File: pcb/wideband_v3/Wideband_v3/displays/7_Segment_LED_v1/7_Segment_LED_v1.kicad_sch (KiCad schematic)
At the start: 31 parts, among them J1 Conn_01x10, U1 4511, U10 74AUC2G04, U2 SM420561N, U3 SM420561N, U4 4511, U5 4511, U6 4511, U7 SM420561N, U8 SM420561N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

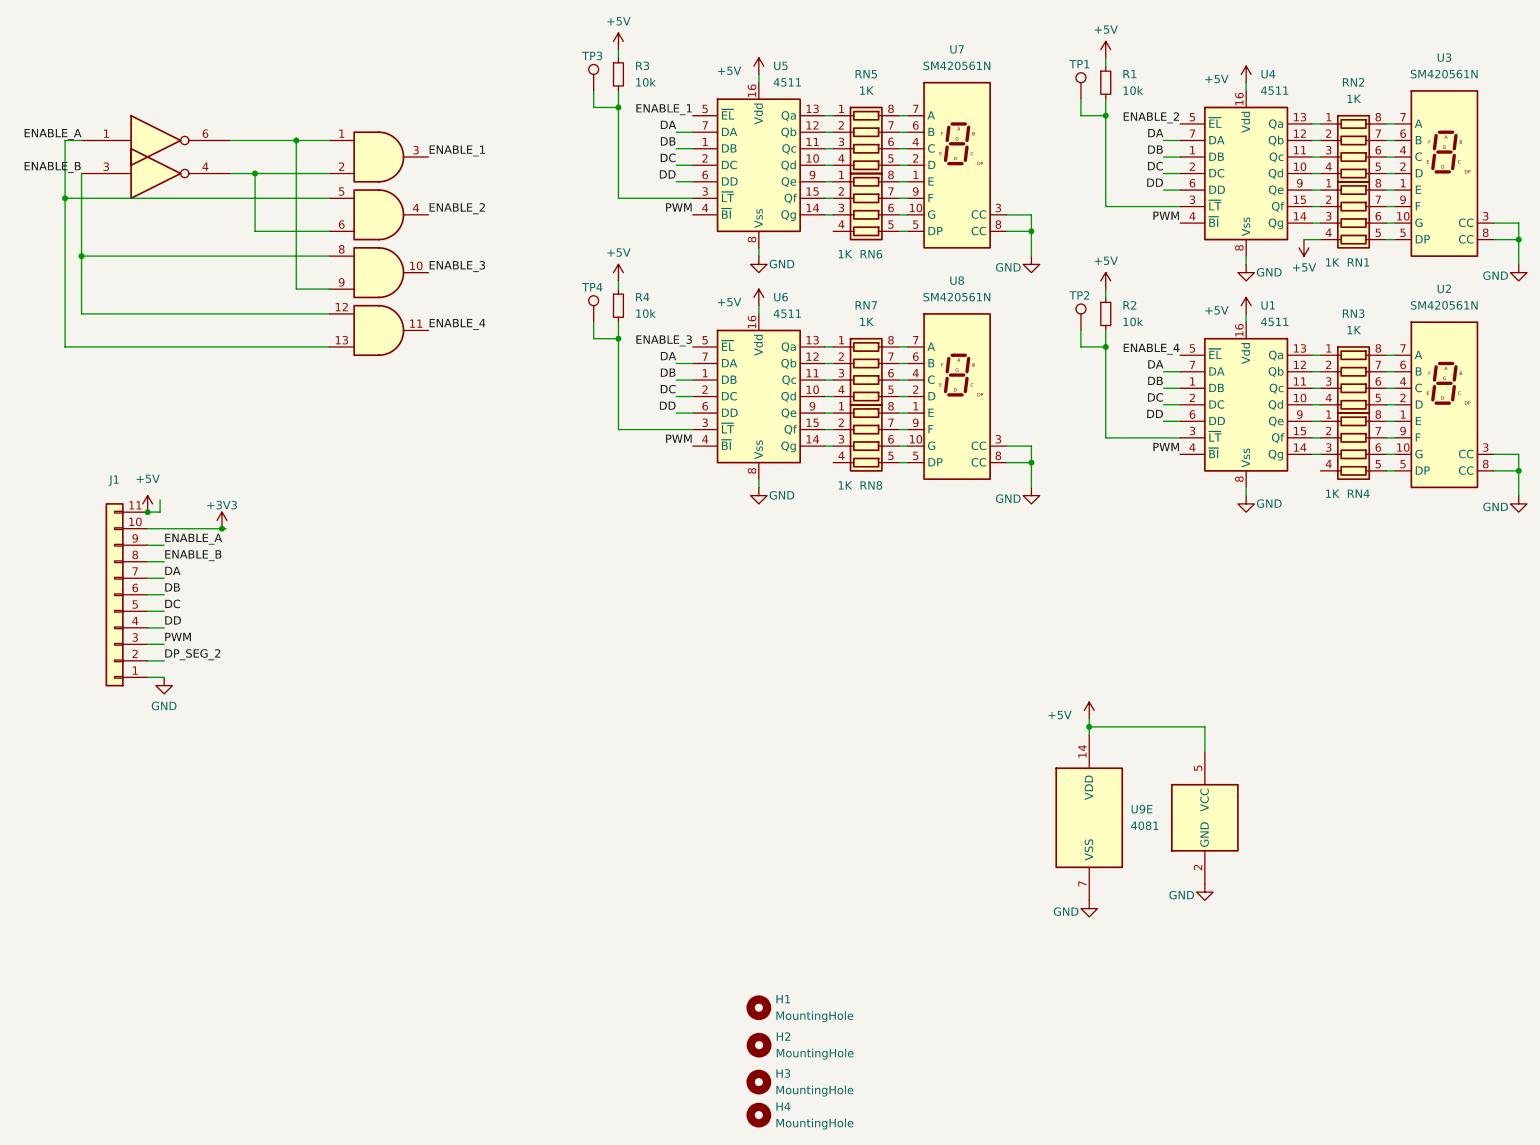
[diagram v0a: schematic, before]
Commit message: rev3, reduce extended component count
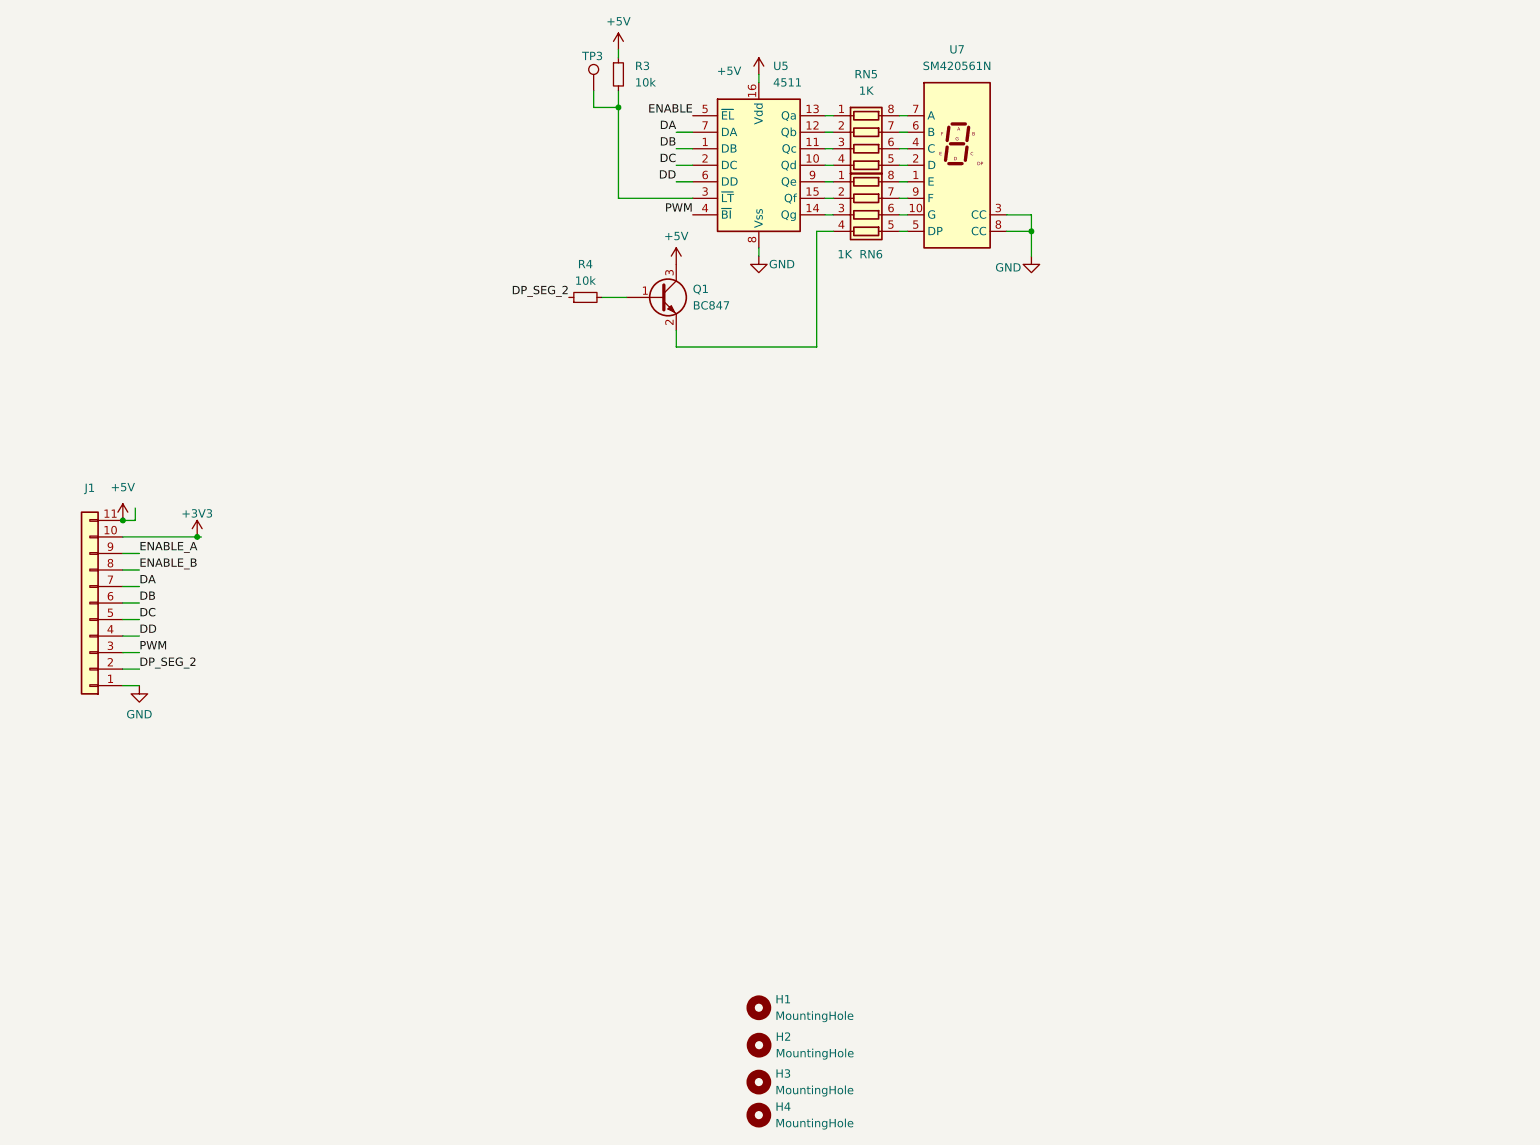
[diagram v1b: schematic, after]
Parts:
- removed R1, R2: 10k, Resistor_SMD:R_0603_1608Metric, symbol Device:R_Small
- removed RN1, RN2, RN3, RN4, RN7, RN8: 1K, Resistor_SMD:R_Array_Convex_4x0603, symbol Device:R_Pack04
- removed TP1, TP2, TP4: TestPoint, TestPoint:TestPoint_Pad_1.0x1.0mm, symbol Connector:TestPoint
- removed U1, U4, U6: 4511, Package_SO:SOP-16_4.55x10.3mm_P1.27mm, symbol 4xxx_IEEE:4511
- removed U10: 74AUC2G04, Package_TO_SOT_SMD:SOT-23-6, symbol 74xGxx:74AUC2G04
- removed U2, U3, U8: SM420561N, Display_7Segment:7SegmentLED_LTS6760_LTS6780, symbol Display_Character:SM420561N
- removed U9: 4081, symbol 4xxx:4081
- added Q1: BC847, Package_TO_SOT_THT:TO-92S_Wide, symbol Transistor_BJT:BC847
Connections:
- net +5V: now also Q1.3 (C); no longer R4.1
- net DP_SEG_2: now also R4.1
- net at R4.2: now also Q1.1 (B)
- net at RN6.4 (R4.1): now also Q1.2 (E)
- net ENABLE_1 renamed ENABLE
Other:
- moved on the sheet: J1

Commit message: update DAC for v3
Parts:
- removed U7: SM420561N, Display_7Segment:SA15-11xxx, symbol Display_Character:SM420561N
- added Q2, Q3, Q4: BC847, Package_TO_SOT_THT:TO-92S_Wide, symbol Transistor_BJT:BC847
- added R1, R2, R5: 10k, Resistor_SMD:R_0603_1608Metric, symbol Device:R_Small
- added U1: ~, symbol New_Library:7seg_3digit
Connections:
- net GND: now also Q2.2 (E), Q3.2 (E), Q4.2 (E)
- net at RN6.8 (R1.2): now also U1.1 (E)
- net at RN6.6 (R3.2): now also U1.5 (G)
- net at RN5.5 (R4.2): now also U1.2 (D)
- net at RN5.6 (R3.2): now also U1.4 (C)
- net at RN6.5 (R4.2): now also U1.3 (DP)
- net at RN5.7 (R2.2): now also U1.7 (B)
- net at RN5.8 (R1.2): now also U1.11 (A)
- net at RN6.7 (R2.2): now also U1.10 (F)
- new net: Q2.3 (C), U1.12 (CC_1)
- new net: Q4.3 (C), U1.8 (CC_3)
- new net: Q3.3 (C), U1.9 (CC_2)
- new net: Q4.1 (B), R5.2
- new net: Q3.1 (B), R2.2
- new net: Q2.1 (B), R1.2
- new net SEG_1: R1.1
- new net SEG_2: R2.1
- new net SEG_3: R5.1

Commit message: update 7seg footprint
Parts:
- removed J1: Conn_01x10, Connector_PinSocket_2.00mm:PinSocket_1x11_P2.00mm_Vertical, symbol Connector_Generic:Conn_01x11
- added J1: Conn_01x14, Connector_PinHeader_2.54mm:PinHeader_2x07_P2.54mm_Vertical, symbol Connector_Generic:Conn_01x14
- Q1, Q2, Q3, Q4: footprint Package_TO_SOT_THT:TO-92S_Wide -> Package_TO_SOT_SMD:SOT-23-3
- U1: footprint (none) -> Library:LED_7SEG
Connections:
- net +5V: now also J1.14 (Pin_14)
- net DA: now also J1.8 (Pin_8)
- net DB: now also J1.7 (Pin_7)
- net DC: now also J1.6 (Pin_6)
- net DD: now also J1.5 (Pin_5)
- net ENABLE: now also J1.12 (Pin_12)
- net GND: now also J1.1 (Pin_1)
- net PWM: now also J1.4 (Pin_4)
- net SEG_1: now also J1.11 (Pin_11)
- net SEG_2: now also J1.10 (Pin_10)
- net SEG_3: now also J1.9 (Pin_9)
- net DP_SEG_2 renamed DP_SEG
- net DP_SEG: now also J1.3 (Pin_3)
- new net +12VA: J1.13 (Pin_13)
- no-connect marks 0 -> 1
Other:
- moved on the sheet: Q1, Q2, Q3, Q4, R1, R2, R3, R4, R5, RN5, RN6, TP3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

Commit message: rev3: update connector on main board
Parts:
- U1: footprint Library:LED_7SEG -> Connector_PinHeader_2.00mm:PinHeader_2x12_P2.00mm_Vertical
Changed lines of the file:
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@@
 			)
 		)
-		(property "Footprint" "Library:LED_7SEG"
+		(property "Footprint" "Connector_PinHeader_2.00mm:PinHeader_2x12_P2.00mm_Vertical"
 			(at 175.26 71.12 0)
 			(effects

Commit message: Bug fixes and enhancements
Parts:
- H1, H2, H3, H4, J1, TP3: now left out of the parts list
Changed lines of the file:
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@@
 		(unit 1)
 		(exclude_from_sim no)
-		(in_bom yes)
+		(in_bom no)
 		(on_board yes)
 		(dnp no)
@@
 		(unit 1)
 		(exclude_from_sim no)
-		(in_bom yes)
+		(in_bom no)
 		(on_board yes)
 		(dnp no)
@@
 		(unit 1)
 		(exclude_from_sim no)
-		(in_bom yes)
+		(in_bom no)
 		(on_board yes)
 		(dnp no)
@@
 		(unit 1)
 		(exclude_from_sim no)
-		(in_bom yes)
+		(in_bom no)
 		(on_board yes)
 		(dnp no)
@@
 		(unit 1)
 		(exclude_from_sim no)
-		(in_bom yes)
+		(in_bom no)
 		(on_board yes)
 		(dnp no)
@@
 		(unit 1)
 		(exclude_from_sim no)
-		(in_bom yes)
-		(on_board yes)
-		(dnp no)
+		(in_bom no)
+		(on_board yes)
+		(dnp no)

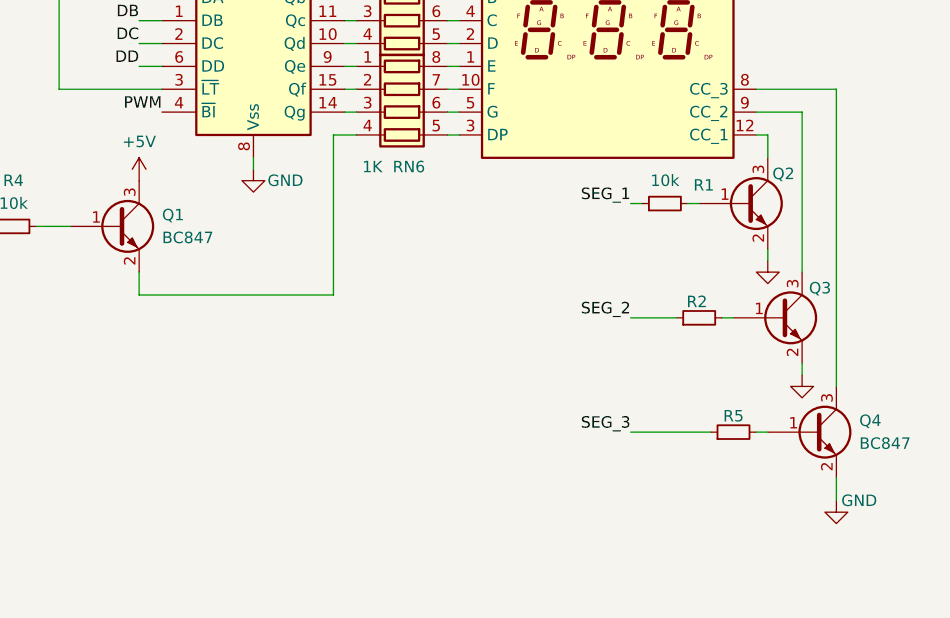
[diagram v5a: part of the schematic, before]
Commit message: update transistors on rev3
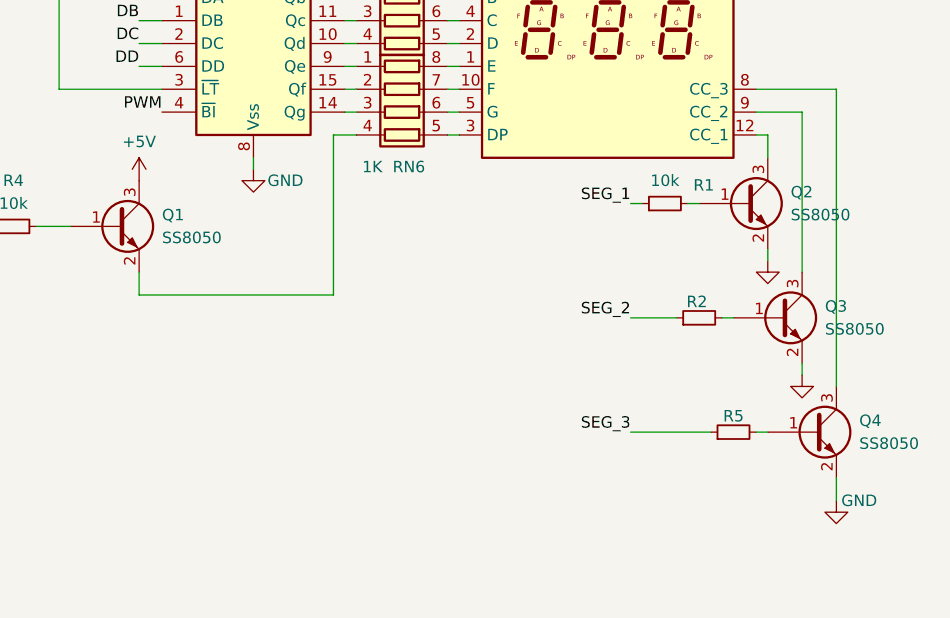
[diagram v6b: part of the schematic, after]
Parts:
- Q1, Q2, Q3, Q4: value BC847 -> SS8050; LCSC (none) -> C2150
